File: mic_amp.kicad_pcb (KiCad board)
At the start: 2 copper layers, 47 x 29 mm, 25 parts

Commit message: filling wanted :)
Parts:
- removed HOLE1: HOLE_METALLED, PCB:Hole3_5_out6mm
- moved D2 22.2 mm to (210.0, 91.3), turned to 180 degrees
- moved R6 19.0 mm to (215.9, 92.1), turned to 270 degrees
- moved R5 8.86 mm to (212.8, 102.5), turned to 180 degrees
- moved R1 8.82 mm to (225.7, 100.4), turned to 90 degrees
- moved F3 7.45 mm to (192.1, 103.7)
- moved C1 6.88 mm to (223.7, 100.4), turned to 90 degrees
- moved R3 6.86 mm to (197.0, 107.8)
- moved R4 6.81 mm to (198.7, 107.8)
- moved F2 6.53 mm to (192.1, 101.9)
- moved F1 6.49 mm to (195.0, 98.7), turned to 90 degrees
- moved C8 6.32 mm to (200.4, 98.7), turned to 90 degrees
- moved XL1 5.86 mm to (225.6, 110.3)
- moved C2 5.60 mm to (218.8, 111.6)
- moved DA1 5.06 mm to (217.8, 115.1), turned to 180 degrees
- moved C7 4.93 mm to (201.8, 102.2), turned to 270 degrees
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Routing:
- net GND: track 0.00 -> 266.6 mm, vias 0 -> 45
- net VDD: track 0.00 -> 72.4 mm
- net Net-(C1-Pad1): track 0.00 -> 28.6 mm, vias 0 -> 2
- net Net-(C4-Pad1): track 0.00 -> 20.7 mm, vias 0 -> 1
- net Net-(R5-Pad3): track 0.00 -> 17.7 mm
- net Net-(C2-Pad1): track 0.00 -> 15.0 mm
- net Net-(C9-Pad2): track 0.00 -> 12.0 mm
- net /MICBIAS: track 0.00 -> 6.73 mm
- net Net-(D1-Pad14): track 0.00 -> 5.21 mm
- net Net-(D2-PadA): track 0.00 -> 4.54 mm
- net Net-(C3-Pad1): track 0.00 -> 4.52 mm
- net Net-(D1-Pad10): track 0.00 -> 4.45 mm
- net Net-(C7-Pad1): track 0.00 -> 4.05 mm
- net Net-(C9-Pad1): track 0.00 -> 3.77 mm
- net Net-(D1-Pad9): track 0.00 -> 3.55 mm
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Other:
- board size 47 x 29 mm -> 41.4 x 28.6 mm

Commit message: plot and drl
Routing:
- net GND: track 266.6 -> 267.1 mm
- added copper zone on B.Cu, net GND
- added copper zone on F.Cu, net GND
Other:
- outline, holes or cut-outs redrawn
- rule pad_to_mask_clearance: 0 -> 0.1
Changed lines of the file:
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@@
   (general
     (links 64)
-    (no_connects 5)
-    (area 189.749999 88.349999 231.250001 117.050001)
+    (no_connects 0)
+    (area 186.846489 88.349999 234.236211 117.087602)
     (thickness 1.6)
-    (drawings 4)
-    (tracks 432)
+    (drawings 8)
+    (tracks 435)
     (zones 0)
     (modules 24)
@@
     (last_trace_width 0.2)
     (trace_clearance 0.2)
-    (zone_clearance 0.508)
+    (zone_clearance 0.3)
     (zone_45_only no)
     (trace_min 0.2)
@@
     (pad_size 1.5 1.5)
     (pad_drill 0.6)
-    (pad_to_mask_clearance 0)
+    (pad_to_mask_clearance 0.1)
     (aux_axis_origin 0 0)
+    (grid_origin 208.5 93.9)
     (visible_elements 7FFFFFFF)
     (pcbplotparams
-      (layerselection 0x00030_80000001)
+      (layerselection 0x010e0_80000001)
       (usegerberextensions false)
       (excludeedgelayer true)
@@
       (outputformat 1)
       (mirror false)
-      (drillshape 1)
+      (drillshape 0)
       (scaleselection 1)
       (outputdirectory ""))
@@
     )
   )
+  (gr_line (start 231.2 106.4) (end 231.2 88.4) (angle 90) (layer Edge.Cuts) (width 0.1))
+  (gr_line (start 231.2 117) (end 231.2 114.2) (angle 90) (layer Edge.Cuts) (width 0.1))
+  (gr_line (start 225.6 114.2) (end 231.2 114.2) (angle 90) (layer Edge.Cuts) (width 0.1))
+  (gr_line (start 225.6 106.4) (end 225.6 114.2) (angle 90) (layer Edge.Cuts) (width 0.1))
+  (gr_line (start 231.2 106.4) (end 225.6 106.4) (angle 90) (layer Edge.Cuts) (width 0.1))
   (gr_line (start 189.8 88.4) (end 231.2 88.4) (angle 90) (layer Edge.Cuts) (width 0.1))
   (gr_line (start 189.8 117) (end 189.8 88.4) (angle 90) (layer Edge.Cuts) (width 0.1))
   (gr_line (start 231.2 117) (end 189.8 117) (angle 90) (layer Edge.Cuts) (width 0.1))
-  (gr_line (start 231.2 88.4) (end 231.2 117) (angle 90) (layer Edge.Cuts) (width 0.1))
   (via (at 222.4998 114.3807) (size 0.8) (layers F.Cu B.Cu) (net 1))
   (via (at 223.1012 116.0876) (size 0.8) (layers F.Cu B.Cu) (net 1))
@@
   (segment (start 226.2008 115.4807) (end 226.3008 115.4807) (width 0.2) (layer F.Cu) (net 1))
   (segment (start 225.0508 115.4807) (end 226.2008 115.4807) (width 0.2) (layer F.Cu) (net 1))
+  (segment (start 208.0121 94.3403) (end 208.8597 94.3403) (width 0.5) (layer B.Cu) (net 2))
+  (via (at 213.6716 90.1959) (size 0.8) (layers F.Cu B.Cu) (net 2))
+  (via (at 218.3043 90.2589) (size 0.8) (layers F.Cu B.Cu) (net 2))
+  (via (at 211.6176 94.3935) (size 0.8) (layers F.Cu B.Cu) (net 2))
+  (segment (start 213.6716 90.1959) (end 211.6176 94.3935) (width 0.5) (layer B.Cu) (net 2))
+  (segment (start 213.6716 90.1959) (end 218.3043 90.2589) (width 0.5) (layer B.Cu) (net 2))
+  (via (at 208.0121 94.3403) (size 0.8) (layers F.Cu B.Cu) (net 2))
+  (segment (start 210.9241 93.7) (end 211.6176 94.3935) (width 0.5) (layer B.Cu) (net 2))
+  (segment (start 209.5 93.7) (end 210.9241 93.7) (width 0.5) (layer B.Cu) (net 2))
+  (segment (start 208.8597 94.3403) (end 209.5 93.7) (width 0.5) (layer B.Cu) (net 2))
   (via (at 224.2013 108.2307) (size 0.8) (layers F.Cu B.Cu) (net 2))
   (via (at 219.8596 110.4395) (size 0.8) (layers F.Cu B.Cu) (net 2))
@@
   (via (at 204.3558 90.141) (size 0.8) (layers F.Cu B.Cu) (net 2))
   (via (at 202.4371 94.5213) (size 0.8) (layers F.Cu B.Cu) (net 2))
-  (via (at 208.0121 94.3403) (size 0.8) (layers F.Cu B.Cu) (net 2))
   (via (at 205.0436 98.3587) (size 0.8) (layers F.Cu B.Cu) (net 2))
   (via (at 204.6816 103.8975) (size 0.8) (layers F.Cu B.Cu) (net 2))
@@
   (via (at 229.1139 96.5619) (size 0.8) (layers F.Cu B.Cu) (net 2))
   (via (at 225.8363 90.8262) (size 0.8) (layers F.Cu B.Cu) (net 2))
-  (via (at 213.6716 90.1959) (size 0.8) (layers F.Cu B.Cu) (net 2))
-  (via (at 218.3043 90.2589) (size 0.8) (layers F.Cu B.Cu) (net 2))
-  (via (at 211.6176 94.3935) (size 0.8) (layers F.Cu B.Cu) (net 2))
-  (segment (start 211.6176 94.3935) (end 208.0121 94.3403) (width 0.5) (layer B.Cu) (net 2))
-  (segment (start 213.6716 90.1959) (end 211.6176 94.3935) (width 0.5) (layer B.Cu) (net 2))
-  (segment (start 218.3043 90.2589) (end 213.6716 90.1959) (width 0.5) (layer B.Cu) (net 2))
   (segment (start 216.7366 98.5759) (end 215.25 95.5243) (width 0.5) (layer B.Cu) (net 2))
   (segment (start 220.0061 96.4043) (end 216.7366 98.5759) (width 0.5) (layer B.Cu) (net 2))
@@
   (segment (start 223.4395 91.1241) (end 224.1132 91.7978) (width 0.2) (layer F.Cu) (net 17))
   (segment (start 221.9623 89.8739) (end 223.4395 91.1241) (width 0.2) (layer F.Cu) (net 17))
+  (zone (net 2) (net_name GND) (layer B.Cu) (hatch edge 0.508)
+    (connect_pads (clearance 0.3))
+    (min_thickness 0.254)
+    (fill yes (arc_segments 32) (thermal_gap 0.25) (thermal_bridge_width 0.508))
+    (polygon
+      (pts
+        (xy 189.8 88.4) (xy 231.2 88.4) (xy 231.2 117) (xy 189.8 117)
+      )
+    )
+  )
+  (zone (net 2) (net_name GND) (layer F.Cu) (hatch edge 0.508)
+    (connect_pads (clearance 0.3))
+    (min_thickness 0.254)
+    (fill yes (arc_segments 32) (thermal_gap 0.25) (thermal_bridge_width 0.508))
+    (polygon
+      (pts
+        (xy 189.8 88.4) (xy 231.2 88.4) (xy 231.2 117) (xy 189.8 117)
+      )
+    )
+  )
 )

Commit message: With 3v battery
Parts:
- removed the C1 at (223.7, 100.4)
- removed the C2 at (218.8, 111.6)
- removed the D1 at (197.1, 103.3)
- removed DA1: NCP662SQ, SOT:SC82AB
- removed the F1 at (195.0, 98.7)
- removed F2: Fuse0R, Resistors:RES_0603_SOLDERFUSE
- removed the R1 at (225.7, 100.4)
- removed the XL2 at (189.9, 92.4)
- added B1: BAT, Installation:BAT_HOLDER_BHX1-2032-SM, F.Cu at (206.5, 103.9)
- added C8: 1u, Capacitors:CAP_0603, B.Cu at (211.1, 110.7)
- added C9: 1u, Capacitors:CAP_0603, B.Cu at (229.2, 109.2)
- added D2: MAX9814, QFN_DFN:DFN14, B.Cu at (192.2, 96.5)
- added D3: BAT54WS, Diodes:SOD323, B.Cu at (211.1, 112.7)
- added HOLE1: HOLE_METALLED, PCB:Hole3d3_out5d5mm, F.Cu at (188.4, 111.6)
- added HOLE2: HOLE_METALLED, PCB:Hole3d3_out5d5mm, F.Cu at (222.5, 96.4)
- added Q1: IRLML9303, SOT:SOT23-3, B.Cu at (223.7, 111.9)
- added Q2: BC848, SOT:SOT23-3, B.Cu at (217.5, 111.9)
- added R2: 0R, Resistors:RES_0603, B.Cu at (187.7, 96.7)
- added R5: 20k, Resistors:RES_0603, B.Cu at (220.7, 111.9)
- added R8: 2k, Resistors:RES_0603, B.Cu at (214.5, 111.9)
- added SW1: SWITCH, BtnsSwitches:SW_SS-1P2T, F.Cu at (230.0, 112.9)
- added XL3: CONN_2, Connectors:PLS-2, F.Cu at (236.5, 112.9)
- C1: renamed from C4; moved to B.Cu
- C2: renamed from C3; moved to B.Cu
- C3: renamed from C5; moved to B.Cu
- C4: renamed from C7; moved to B.Cu
- C5: renamed from C6; value 0.1u -> 10u; moved to B.Cu
- C6: renamed from C8; value 1u -> 0.1u; moved to B.Cu
- C7: renamed from C9; moved to B.Cu
- F1: renamed from F3; moved to B.Cu
- R1: renamed from R2; moved to B.Cu
- R3: value 150k -> DNM; moved to B.Cu
- R4: value 100k -> 2k; moved to B.Cu
- R6: value 1k -> 2k; moved to B.Cu
- XL1: value USB_MINI_B -> CONN_2; footprint Connectors:USBmicro_MOLEX_WM17142 -> Connectors:PLS-2
- XL2: renamed from XL3; moved to B.Cu
- moved XL1 39.4 mm to (186.9, 102.7), turned to 270 degrees
- moved R4 33.2 mm to (229.5, 95.4), turned to 0 degrees
- moved C7 26.2 mm to (222.9, 108.5), turned to 0 degrees
- moved D1 25.8 mm to (235.5, 95.4), turned to 0 degrees
- moved R7 19.8 mm to (232.5, 103.9), turned to 270 degrees
- moved R6 17.1 mm to (215.6, 109.2), turned to 180 degrees
- moved R3 15.9 mm to (187.7, 94.9), turned to 180 degrees
- moved XL2 13.7 mm to (238.5, 103.9)
- moved C3 12.7 mm to (197.8, 95.4), turned to 0 degrees
- moved R1 10.8 mm to (188.6, 99.3)
- moved C1 9.79 mm to (187.0, 99.3), turned to 90 degrees
- moved C5 7.92 mm to (214.7, 103.9), turned to 180 degrees
- moved C2 7.13 mm to (197.8, 102.2), turned to 0 degrees
- moved C4 6.59 mm to (197.8, 97.0), turned to 0 degrees
- moved F1 3.88 mm to (192.3, 99.8), turned to 0 degrees
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- renumbered D2 to D1, R5 to R7
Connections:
- C1 pad 1: Net-(C4-Pad1) (its old number) -> Net-(C1-Pad1)
- C1 pad 2: /MICIN -> Net-(C1-Pad2)
- C5 pad 1: VDD -> /BAT_IN
- D1 pad A: Net-(D2-PadA) -> Net-(D1-PadA)
- R1 pad 1: Net-(C4-Pad1) (its old number) -> Net-(C1-Pad1)
- R3 pad 1: /MICBIAS -> /MICIN
- R3 pad 2: Net-(D1-Pad14) -> GND
- R4 pad 1: Net-(D1-Pad14) -> VDD
- R4 pad 2: GND -> Net-(D1-PadA)
- R6 pad 1: Net-(D2-PadA) -> Net-(Q2-Pad1)
- R6 pad 2: VDD -> Net-(C8-Pad1)
- XL1 pad 1: Net-(C2-Pad1) (its old number) -> Net-(C1-Pad1)
- XL1 pad 2: Net-(XL1-Pad2) -> GND
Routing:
- net /BAT_IN: track 0.00 -> 62.8 mm, vias 0 -> 1
- net Net-(C9-Pad2): track 0.00 -> 32.7 mm
- net GND: track 267.1 -> 234.8 mm, vias 45 -> 32
- net Net-(C7-Pad1): track 3.77 -> 32.3 mm
- net Net-(C1-Pad1): track 28.6 -> 4.25 mm, vias 2 -> 0
- net Net-(C4-Pad1) (its old number): track 20.7 -> 0.00 mm, vias 1 -> 0
- net Net-(C2-Pad1) (its old number): track 15.0 -> 0.00 mm
- net Net-(C7-Pad2): track 12.0 -> 2.79 mm
- net Net-(C8-Pad1): track 0.00 -> 7.72 mm
- net Net-(C2-Pad1): track 4.52 -> 12.2 mm
- net VDD: track 72.4 -> 65.0 mm, vias 0 -> 3
- net (no net): track 0.00 -> 5.38 mm, vias 0 -> 1
- net Net-(Q1-Pad1): track 0.00 -> 5.24 mm
- net Net-(D1-Pad14): track 5.21 -> 0.00 mm
- net /MICIN: track 3.12 -> 7.83 mm, vias 0 -> 2
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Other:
- board size 41.4 x 28.6 mm -> 53.5 x 22 mm
- board text added: "F1: Soldered => 50dB Not soldered => 60dB"
- board text added: "StetoAmp 2"

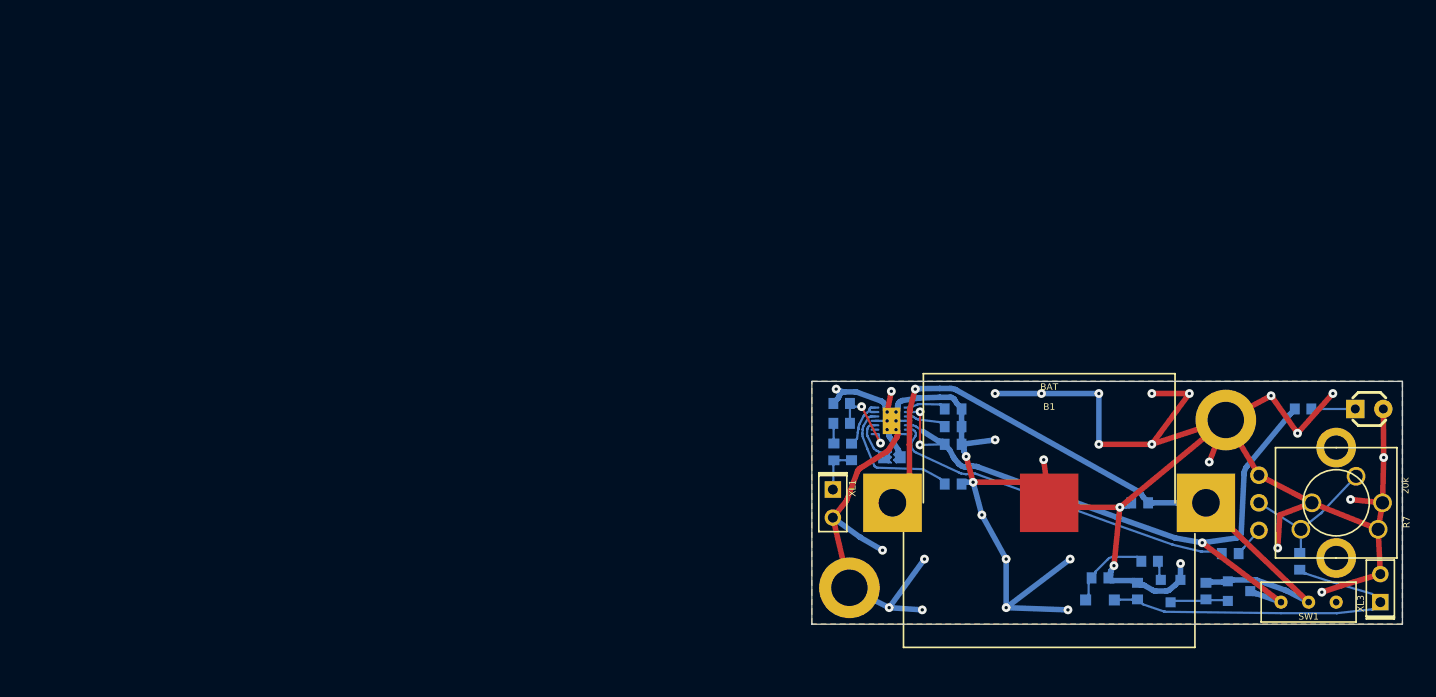
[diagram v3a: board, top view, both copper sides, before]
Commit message: 2xAAA sch
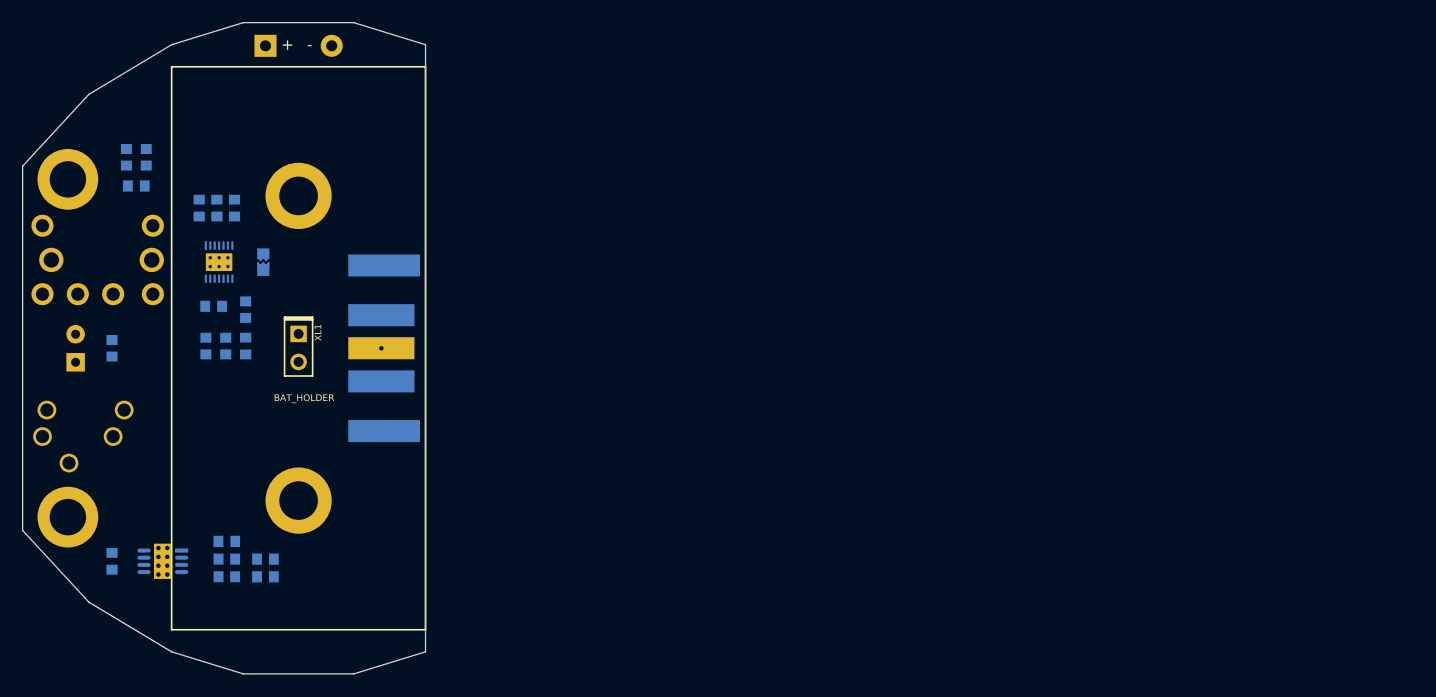
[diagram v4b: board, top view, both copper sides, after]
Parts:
- removed the C5 at (214.7, 103.9)
- removed D3: BAT54WS, Diodes:SOD323
- removed Q1: IRLML9303, SOT:SOT23-3
- removed Q2: BC848, SOT:SOT23-3
- removed SW1: SWITCH, BtnsSwitches:SW_SS-1P2T
- added C10: 1u, Capacitors:CAP_0603, B.Cu at (121.6, 109.2)
- added C6: 1u, Capacitors:CAP_0603, B.Cu at (135.5, 110.6)
- added DA1: TPA6211, QFN_DFN:DRB8, B.Cu at (126.2, 109.2)
- added R8: 0R, Resistors:RES_0603, B.Cu at (124.7, 72.6)
- B1: value BAT -> BAT_HOLDER; footprint Installation:BAT_HOLDER_BHX1-2032-SM -> Installation:BATTERY_AAA_X2
- D1: moved to B.Cu
- R5: value 20k -> RVarWSw; footprint Resistors:RES_0603 -> Resistors:RVar_SP3
- R6: value 2k -> 10k
- R7: value 20k -> 10k; footprint Resistors:VAR_PTV09A-4 -> Resistors:RES_0603; moved to B.Cu
- XL2: value CONN_AUDIO_SIMPLE -> AudioJackSimple
- XL3: value CONN_2 -> AudioJackSimple_x4; footprint Connectors:PLS-2 -> Connectors:Audio_ST013; moved to B.Cu
- moved XL3 126.8 mm to (113.5, 81.9), turned to 180 degrees
- moved XL2 125.1 mm to (113.5, 97.9), turned to 180 degrees
- moved D1 117.3 mm to (118.3, 89.9), turned to 90 degrees
- moved C9 110.7 mm to (123.8, 75.2), turned to 180 degrees
- moved R4 108.0 mm to (121.6, 89.9), turned to 270 degrees
- moved HOLE2 107.1 mm to (117.6, 74.6)
- moved R7 100.6 mm to (132.0, 109.0), turned to 180 degrees
- moved R9 99.7 mm to (122.9, 72.6)
- moved C7 87.4 mm to (135.5, 109.0)
- moved R6 83.6 mm to (132.0, 110.6)
- moved C8 79.2 mm to (132.0, 107.4)
- moved R5 74.0 mm to (150.0, 89.9), turned to 90 degrees
- moved HOLE1 71.1 mm to (117.6, 105.2)
- moved C3 70.7 mm to (129.5, 77.2), turned to 90 degrees
- moved C4 69.6 mm to (131.1, 77.2), turned to 90 degrees
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- renumbered C6 to C5, R8 to R9
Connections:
- B1 pad A: /BAT_IN -> +BATT
- C5 pad 1: VDD -> +3.3V
- C7 pad 2: Net-(C7-Pad2) -> GND
- D2 pad 2: VDD -> +3.3V
- D2 pad 5: VDD -> +3.3V
- D2 pad 6: Net-(C7-Pad1) -> /Output
- R4 pad 1: VDD -> +3.3V
- R5 pad 1: /BAT_IN -> /Output
- R5 pad 2: Net-(Q1-Pad1) -> GND
- R6 pad 2: Net-(C8-Pad1) -> Net-(DA1-Pad4)
- R7 pad 1: GND -> Net-(C7-Pad1)
- R7 pad 2: Net-(C7-Pad2) -> Net-(DA1-Pad3)
- XL2 pad 1: GND -> Net-(DA1-Pad8)
- XL2 pad 2: Net-(C9-Pad1) -> Net-(DA1-Pad5)
- XL2 pad 3: Net-(C9-Pad1) -> Net-(DA1-Pad5)
- XL2 pad H: GND -> Net-(XL2-PadH)
- XL3 pad 1: Net-(C9-Pad2) -> GND
- XL3 pad 2: GND -> (no net)
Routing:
- net GND: track 234.8 -> 0.00 mm, vias 32 -> 0
- net VDD: track 65.0 -> 0.00 mm, vias 3 -> 0
- net /BAT_IN: track 62.8 -> 0.00 mm, vias 1 -> 0
- net Net-(C9-Pad2): track 32.7 -> 0.00 mm
- net Net-(C7-Pad1): track 32.3 -> 0.00 mm
- net Net-(C9-Pad1): track 13.6 -> 0.00 mm
- net Net-(C2-Pad1): track 12.2 -> 0.00 mm
- net /MICIN: track 7.83 -> 0.00 mm, vias 2 -> 0
- net Net-(C8-Pad1): track 7.72 -> 0.00 mm
- net (no net): track 5.38 -> 0.00 mm, vias 1 -> 0
- net Net-(Q1-Pad1): track 5.24 -> 0.00 mm
- net /MICBIAS: track 4.85 -> 0.00 mm
- net Net-(C1-Pad1): track 4.25 -> 0.00 mm
- net Net-(D2-Pad10): track 4.00 -> 0.00 mm
- net Net-(D1-PadA): track 3.98 -> 0.00 mm
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- removed copper zone on B.Cu, net GND
- removed copper zone on F.Cu, net GND
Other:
- board size 53.5 x 22 mm -> 36.5 x 59 mm

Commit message: + Pcb sent to manufacturing
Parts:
- added C11: 10u, Capacitors:CAP_0603, B.Cu at (141.7, 100.3)
- added C12: 0.1u, Capacitors:CAP_0603, B.Cu at (141.7, 102.3)
- added C13: 10u, Capacitors:CAP_0603, B.Cu at (137.5, 109.9)
- added C14: 10u, Capacitors:CAP_0603, B.Cu at (137.5, 103.9)
- added D3: BAT54WS, Diodes:SOD323, B.Cu at (143.1, 109.3)
- added DA2: NCP140x, SOT:SOT23-5, B.Cu at (140.5, 109.3)
- added HOLE3: HOLE_METALLED, PCB:Hole3d3_out5d5mm, F.Cu at (148.0, 107.9)
- added HOLE4: HOLE_METALLED, PCB:Hole3d3_out5d5mm, F.Cu at (148.0, 71.9)
- added L1: 22uH, Inductors:IND_1210_LQH32C, B.Cu at (141.7, 105.1)
- added L2: BLM15AG102, Inductors:IND_0402, B.Cu at (137.5, 106.9)
- B1: value BAT_HOLDER -> BAT; footprint Installation:BATTERY_AAA_X2 -> Installation:BATTERY_AAA_X1
- R5: footprint Resistors:RVar_SP3 -> Resistors:RVar_SP3_R
- moved C6 14.1 mm to (135.3, 96.5), turned to 270 degrees
- moved C7 12.7 mm to (133.3, 96.5), turned to 90 degrees
- moved R3 11.8 mm to (140.4, 84.0)
- moved HOLE1 11.7 mm to (129.0, 107.9)
- moved HOLE2 11.7 mm to (129.0, 71.9)
- moved R6 11.2 mm to (135.3, 99.9), turned to 270 degrees
- moved C5 9.64 mm to (140.4, 71.4)
- moved C4 9.32 mm to (138.4, 71.4)
- moved C2 9.27 mm to (138.4, 80.8), turned to 270 degrees
- moved D2 9.26 mm to (138.6, 76.4)
- moved R7 9.19 mm to (133.3, 99.9), turned to 270 degrees
- moved C3 9.01 mm to (136.4, 71.4)
- moved R2 8.65 mm to (138.4, 84.0)
- moved R5 7.50 mm to (157.5, 89.9)
- moved DA1 6.82 mm to (124.5, 102.6)
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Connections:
- B1 pad A: +BATT -> /BAT_IN
- R5 pad 4: +BATT -> /BAT_IN
- R5 pad 5: +3.3V -> +BATT
- XL2 pad H: Net-(XL2-PadH) -> GND
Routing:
- net GND: track 0.00 -> 366.1 mm, vias 0 -> 52
- net +3.3V: track 0.00 -> 83.0 mm, vias 0 -> 5
- net /Output: track 0.00 -> 29.8 mm, vias 0 -> 2
- net /BAT_IN: track 0.00 -> 18.7 mm
- net Net-(C6-Pad1): track 0.00 -> 13.6 mm, vias 0 -> 1
- net Net-(C9-Pad2): track 0.00 -> 13.4 mm
- net Net-(DA1-Pad5): track 0.00 -> 13.0 mm, vias 0 -> 1
- net +BATT: track 0.00 -> 10.8 mm
- net Net-(DA1-Pad4): track 0.00 -> 9.99 mm
- net Net-(C1-Pad1): track 0.00 -> 8.71 mm
- net /MICIN: track 0.00 -> 8.53 mm
- net /3v3unfil: track 0.00 -> 8.14 mm
- net Net-(DA1-Pad3): track 0.00 -> 7.98 mm
- net Net-(DA1-Pad8): track 0.00 -> 7.95 mm
- net Net-(XL3-Pad3): track 0.00 -> 7.13 mm
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- added copper zone on B.Cu, net GND
- added copper zone on F.Cu, net GND
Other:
- board size 36.5 x 59 mm -> 33.6 x 51 mm
- board text added: "Output"
- board text removed: "StetoAmp 2"
